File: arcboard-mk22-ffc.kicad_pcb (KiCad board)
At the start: 2 copper layers, 313 x 104.2 mm, 23 parts, among them J10 Conn_01x60, J7 Conn_01x04, J8 Conn_01x04

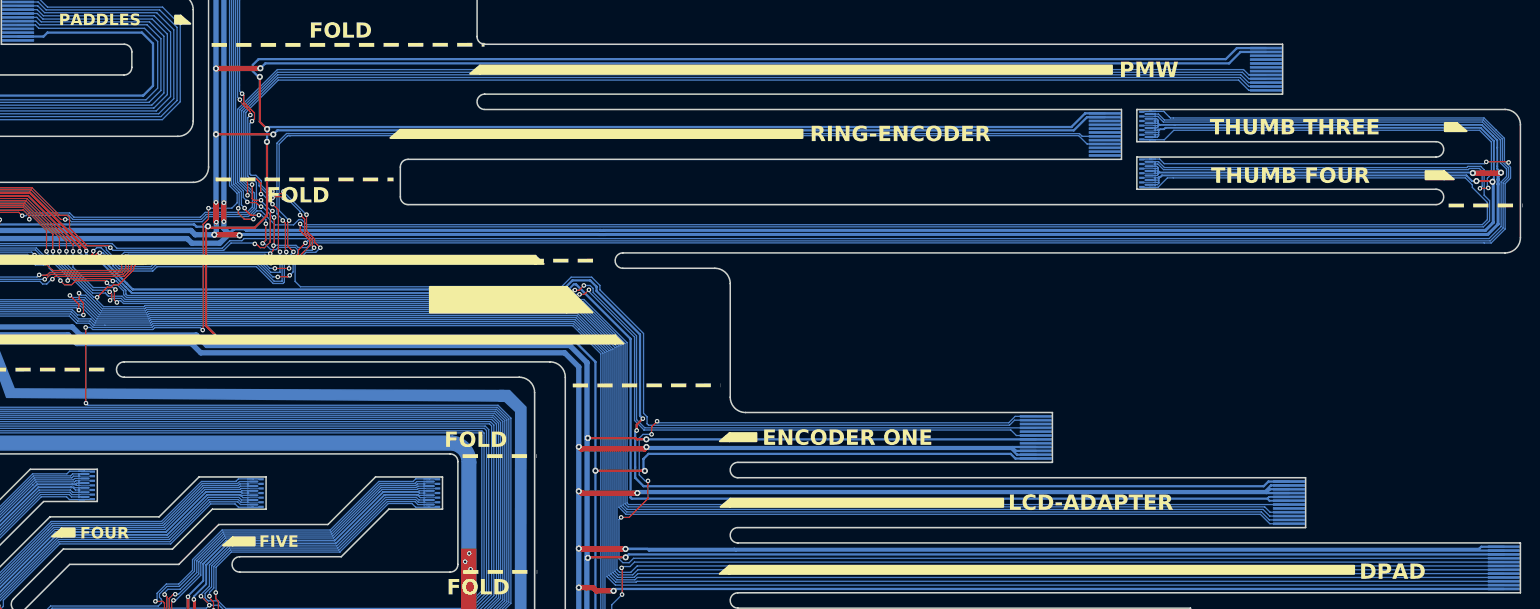
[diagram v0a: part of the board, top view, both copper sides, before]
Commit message: fixing the reversed pinouts for pmw and lcd-adapter
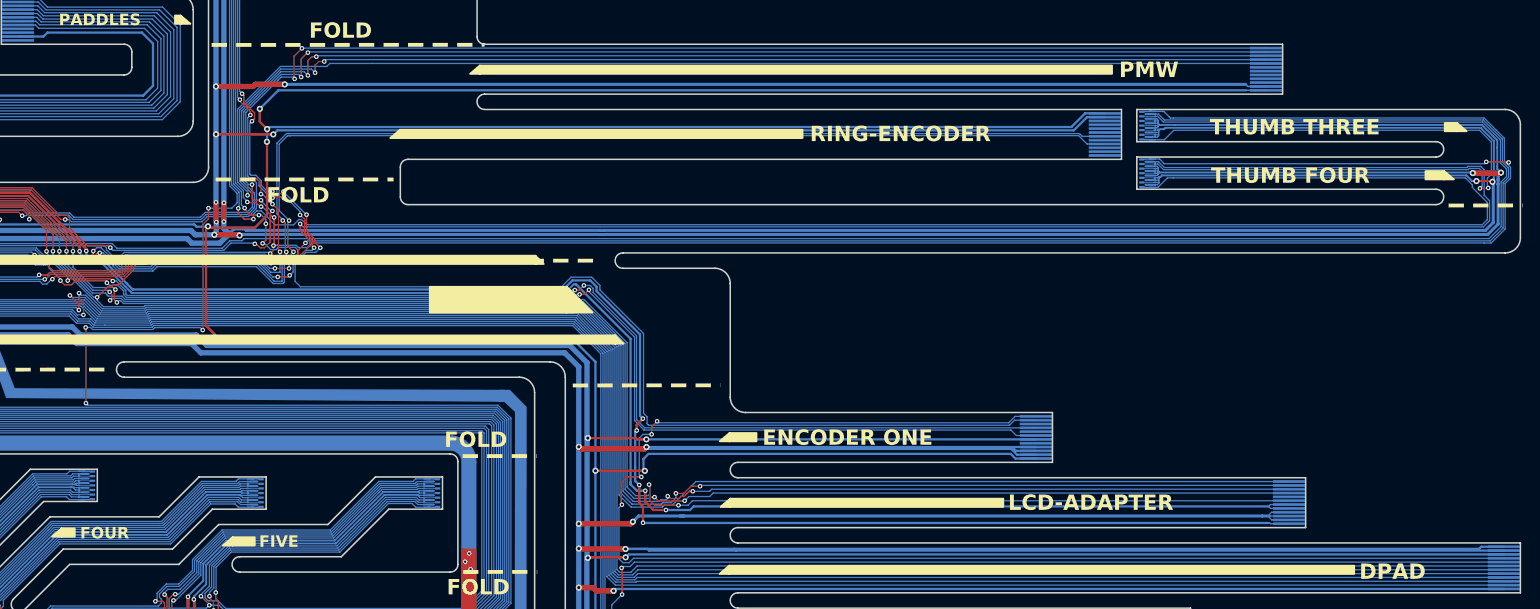
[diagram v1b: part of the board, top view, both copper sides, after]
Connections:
- LCD1 pad 1: SPI1_CLK -> LCD_3V3
- LCD1 pad 10: GND -> LCD_CS
- LCD1 pad 11: GND -> SPI1_MOSI
- LCD1 pad 12: LCD_3V3 -> SPI1_CLK
- LCD1 pad 2: SPI1_MOSI -> GND
- LCD1 pad 3: LCD_CS -> GND
- LCD1 pad 4: LCD_DC -> GND
- LCD1 pad 5: unconnected-(LCD1-Pin_5-Pad5) -> LCD_BL
- LCD1 pad 6: LCD_RST -> LCD_BL
- LCD1 pad 7: LCD_BL -> LCD_RST
- LCD1 pad 8: LCD_BL -> unconnected-(LCD1-Pin_8-Pad8)
- LCD1 pad 9: GND -> LCD_DC
- PMW1 pad 1: SPI1_CLK -> +3V3
- PMW1 pad 10: unconnected-(PMW1-Pin_10-Pad10) -> PMW_CS
- PMW1 pad 11: GND -> SPI1_MISO
- PMW1 pad 12: +3V3 -> SPI1_CLK
- PMW1 pad 2: SPI1_MISO -> GND
- PMW1 pad 3: PMW_CS -> unconnected-(PMW1-Pin_3-Pad3)
- PMW1 pad 4: PMW_MOTION -> unconnected-(PMW1-Pin_4-Pad4)
- PMW1 pad 5: SPI1_MOSI -> unconnected-(PMW1-Pin_5-Pad5)
- PMW1 pad 8: unconnected-(PMW1-Pin_8-Pad8) -> SPI1_MOSI
- PMW1 pad 9: unconnected-(PMW1-Pin_9-Pad9) -> PMW_MOTION
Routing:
- net GND: track 3095.3 -> 3013.0 mm
- net +3V3: track 651.3 -> 644.3 mm
- net LCD_3V3: track 310.9 -> 315.5 mm, vias 4 -> 6
- net SPI1_CLK: track 510.5 -> 513.3 mm, vias 4 -> 6
- net SPI1_MISO: track 308.9 -> 311.4 mm, vias 6 -> 8
- net LCD_RST: track 312.3 -> 314.5 mm, vias 2 -> 4
- net PMW_CS: track 299.0 -> 301.2 mm, vias 2 -> 4
- net PMW_MOTION: track 298.4 -> 299.7 mm, vias 2 -> 4
- net LCD_DC: track 313.7 -> 312.5 mm, vias 4 -> 6
- net LCD_CS: track 313.6 -> 312.9 mm, vias 4 -> 6
- net LCD_BL: track 314.0 -> 314.4 mm, vias 2 -> 4
- net SPI1_MOSI: track 505.0 -> 504.6 mm, vias 8 -> 10
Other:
- board text added: "Stiffener notes: All single-row finger (0.5mm-spacing) must be 0.3mm total thickness. All double-row finger (0.3mm spacing) must be 0.2mm total thickness. All stiffeners are polyimide."

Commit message: updating ring-led-pcb pinouts
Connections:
- J8 pad 2: ENC2_DO -> +5V
- J8 pad 3: Main_LED_OUT -> ENC2_DO
- J8 pad 4: +5V -> Main_LED_OUT
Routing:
- net ENC2_DO: track 172.9 -> 171.9 mm

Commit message: fixing silkscreen
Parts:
- removed LOGO2: **REF, kicad-libraries:awesome-logo
- added LOGO1: **REF, kicad-libraries:awesome-logo, B.Cu at (181.1, 15.3)
- moved LOGO1 171.5 mm to (181.1, 15.3)
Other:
- board text added: "0"
- board text added: "1"
- board text added: "2"
- board text added: "3"
- board text added: "4"
- board text added: "5"
- board text added: "COLUMNS"
- board text added: "PADL"
- board text added: "github.com/christrotter/arcboard-stm32-mk2"
- board text added: "this side up: left"
- board text added: "this side up: right"
- board text removed: "FIVE"
- board text removed: "FOLD"
- board text removed: "FOUR"
- board text removed: "LEFT"
- board text removed: "ONE"
- board text removed: "PADDLES"
- board text removed: "RIGHT"
- board text removed: "THREE"
- board text removed: "TWO"
- board text removed: "pairs with: github.com/christrotter/arcboard-stm32-mk2"
- board text removed: "zero"

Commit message: ordered this
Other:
- board text added: "Stiffener notes: All single-row finger (0.5mm-spacing) must be 0.3mm total thickness - including stiffener. All double-row finger (0.3mm spacing) must be 0.2mm total thickness - including stiffener. All stiffeners are polyimide."
- board text removed: "Stiffener notes: All single-row finger (0.5mm-spacing) must be 0.3mm total thickness. All double-row finger (0.3mm spacing) must be 0.2mm total thickness. All stiffeners are polyimide."
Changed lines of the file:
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@@
 		(layer "F.SilkS")
 	)
+	(gr_line
+		(start 176.3 51.100656)
+		(end 183.06 51.119344)
+		(stroke
+			(width 0.5)
+			(type dot)
+		)
+		(layer "F.SilkS")
+	)
 	(gr_arc
 		(start 39.7437 46.1)
@@
 		(layer "F.SilkS")
 	)
+	(gr_line
+		(start 176.36 34.74)
+		(end 183.12 34.758688)
+		(stroke
+			(width 0.5)
+			(type dot)
+		)
+		(layer "F.SilkS")
+	)
 	(gr_poly
 		(pts
@@
 	)
 	(gr_line
+		(start 190.82 53.301312)
+		(end 209.26 53.278688)
+		(stroke
+			(width 0.5)
+			(type dot)
+		)
+		(layer "F.SilkS")
+	)
+	(gr_line
 		(start 269.5 56)
 		(end 269.5 61.5)
@@
 	)
 	(gr_line
+		(start 176.3 51.250656)
+		(end 183.16 51.259344)
+		(stroke
+			(width 0.5)
+			(type dot)
+		)
+		(layer "B.SilkS")
+	)
+	(gr_line
 		(start 268.230761 64.65)
 		(end 211 64.65)
@@
 	)
 	(gr_line
+		(start 190.82 53.451312)
+		(end 209.26 53.428688)
+		(stroke
+			(width 0.5)
+			(type dot)
+		)
+		(layer "B.SilkS")
+	)
+	(gr_line
 		(start 112.35 -21.95)
 		(end 7.2 -21.95)
@@
 		(layer "B.SilkS")
 	)
+	(gr_line
+		(start 176.36 34.89)
+		(end 183.22 34.898688)
+		(stroke
+			(width 0.5)
+			(type dot)
+		)
+		(layer "B.SilkS")
+	)
 	(gr_rect
 		(start 136.425 -20.61)
@@
 		)
 	)
-	(gr_text "Stiffener notes:\nAll single-row finger (0.5mm-spacing) must be 0.3mm total thickness.\nAll double-row finger (0.3mm spacing) must be 0.2mm total thickness.\nAll stiffeners are polyimide."
+	(gr_text "Stiffener notes:\nAll single-row finger (0.5mm-spacing) must be 0.3mm total thickness - including stiffener.\nAll double-row finger (0.3mm spacing) must be 0.2mm total thickness - including stiffener.\nAll stiffeners are polyimide."
 		(at 2.04 -49.07 0)
 		(layer "Cmts.User")
@@
 	)
 	(segment
-		(start 203.92 43.49)
-		(end 203.46 43.49)
-		(width 0.4)
-		(layer "B.Cu")
-		(net 7)
-	)
-	(segment
 		(start 76.364 42.636)
 		(end 79.65 39.35)
@@
 	)
 	(segment
-		(start 151.03322 -13.28678)
-		(end 151.07644 -13.33)
-		(width 0.13)
-		(layer "B.Cu")
-		(net 21)
-	)
-	(segment
 		(start 123.32 4.84)
 		(end 123.84 4.84)
@@
 		(layer "B.Cu")
 		(net 36)
-	)
-	(segment
-		(start 163.37 -15.5)
-		(end 163.29911 -15.5)
-		(width 0.13)
-		(layer "B.Cu")
-		(net 36)
